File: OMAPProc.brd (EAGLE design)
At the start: 49.8 x 23.2 mm, 11 parts

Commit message: Pre-reinstall commit
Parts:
- removed C30, C31, C32, C33: 0.1uF, SparkFun:0402-CAP
- removed JP11: MPCS6PH, stan:MOLEX-PICO_CLASP_S6P
- removed R18: 4.7k, rcl:R0402
- removed R19, R20: 1.5k, rcl:R0402
- removed SHIFT1: TXS0108E, user:PW_R-PDSO-G20
- added C1, C15, C16, C17, C18, C19, C2, C21, C22, C3, C8: 0.1uF, biomimetic:0402-CAP
- added C10, C11, C12, C13, C14, C4, C5, C6, C9: 1uF, biomimetic:0402-CAP
- added C20: (no value), biomimetic:0603-CAP
- added C7: 22uF, biomimetic:0603-CAP
- added CAM2: ECAM50_5642_MOD, biomimetic:XF2W-2415-1A
- added IC1: MIC5335-SPYMT, biomimetic:MLF-6
- added IC2: MIC5335-MGYMT, biomimetic:MLF-6
- added IC3: TXS0108ERGY, biomimetic:R-PVQFN-N20
- added JP1: Console, biomimetic:MOLEX_503480-0600
- added JP2: ImageProc, biomimetic:MOLEX_503480-0600
- added R1, R2: 1.5k, biomimetic:0402-RES
- added R3, R4, R5, R6, R7: 10k, biomimetic:0402-RES
- added R8: DNP, biomimetic:0402-RES
- added S1: SW_RESET, SparkFun-Electromechanical:TACTILE-SWITCH-1101NE
- added S2: SW_PWRON, SparkFun-Electromechanical:TACTILE-SWITCH-1101NE
- added SDCARD1: MICROSD, biomimetic:AVX_045138008010890+
- CAM1: value AXK7L28227G(LI-VM01CM) -> LI-VM01CM; device user:AXK7L28227G -> biomimetic:AXK7L28227G
- moved SOM1 29.8 mm to (35.8, 11.7), turned to 0 degrees
- moved CAM1 0.89 mm to (9.75, 11.3)
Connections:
- removed net N$18: SHIFT1.20
- removed net N$22: SHIFT1.18
- removed net N$27: SHIFT1.17
- removed net N$30: SHIFT1.16
- removed net N$31: SHIFT1.15
- removed net N$33: SHIFT1.14
- removed net N$34: SHIFT1.13
- removed net N$35: SHIFT1.12
- removed net OMAP_1.8V: C30.1, C32.1, CAM1.10, CAM1.11, R18.2, R19.2, R20.2, SHIFT1.10, SHIFT1.2
- removed net OMAP_3.0V: C31.2, CAM1.13
- removed net OMAP_3.3V: C33.1, SHIFT1.19
- removed net OMAP_GND: C30.2, C31.1, C32.2, C33.2, CAM1.12, CAM1.17, JP11.2, R18.1, SHIFT1.11
- removed net OMAP_SPI2_CLK: SHIFT1.1
- removed net OMAP_SPI2_CS0: SHIFT1.5
- removed net OMAP_SPI2_CS1: SHIFT1.6
- removed net OMAP_SPI2_IRQ: SHIFT1.7
- removed net OMAP_SPI2_SIMO: SHIFT1.3
- removed net OMAP_SPI2_SOMI: SHIFT1.4
- removed net OMAP_SPI4_CLK: SHIFT1.8
- removed net OMAP_SPI4_SIMO: SHIFT1.9
- removed net TERMINAL_CTS: JP11.6
- removed net TERMINAL_RTS: JP11.5
- removed net TERMINAL_RX: JP11.3
- removed net TERMINAL_TX: JP11.4
- removed net V-: SOM1.J1.100, SOM1.J1.12, SOM1.J1.17, SOM1.J1.22, SOM1.J1.27, SOM1.J1.61, SOM1.J1.85, SOM1.J2.1, SOM1.J2.2, SOM1.J2.27, SOM1.J2.30, SOM1.J2.59, SOM1.J2.62, SOM1.J2.90, SOM1.J2.99
- new net !RESET: CAM1.20, CAM2.6, SOM1.J2.6
- new net 1.8V: C1.2, C11.1, C15.1, C19.1, C2.1, C4.1, C5.2, CAM1.10, CAM1.11, CAM2.11, IC2.5, IC3.10, IC3.2, R1.1, R2.1
- new net 2.8V: C10.1, C18.1, C3.1, C6.1, CAM1.13, CAM2.4, IC2.6
- new net 3.0V: C14.1, IC1.5
- new net 3.3V: C13.1, C16.1, C17.1, CAM2.23, IC1.6, IC3.19
- new net GND: C1.1, C10.2, C11.2, C12.1, C13.2, C14.2, C15.2, C16.2, C17.2, C18.2, C19.2, C2.2, C20.2, C21.2, C22.2, C3.2, C4.2, C5.1, C6.2, C7.2, C8.2, C9.1, CAM1.12, CAM1.17, CAM1.21, CAM2.15, CAM2.2, CAM2.24, CAM2.8, IC1.2, IC1.EPAD, IC2.2, IC2.EPAD, IC3.11, IC3.EPAD, JP1.1, JP2.3, JP2.5, SDCARD1.6, SDCARD1.CASE1, SDCARD1.CASE2, SDCARD1.CASE3, SDCARD1.CASE4, SDCARD1.COM, SOM1.J1.100, SOM1.J1.12, SOM1.J1.17, SOM1.J1.22, SOM1.J1.27, SOM1.J1.61, SOM1.J1.85, SOM1.J2.1, SOM1.J2.2, SOM1.J2.27, SOM1.J2.30, SOM1.J2.59, SOM1.J2.62, SOM1.J2.90, SOM1.J2.99
- new net MSTR_NRST: C21.1, S1.P$1, SOM1.J2.92
- new net N$3: S1.P$2, S2.P$2
- new net PWRON: C22.1, S2.P$1, SOM1.J1.5
- new net SD1_CD: R8.1, SDCARD1.CD, SOM1.J2.54
- new net SD1_CLK: SDCARD1.5, SOM1.J2.32
- new net SD1_CMD: R3.1, SDCARD1.3, SOM1.J2.42
- new net SD1_DATA0: R4.1, SDCARD1.7, SOM1.J2.48
- new net SD1_DATA1: R5.1, SDCARD1.8, SOM1.J2.46
- new net SD1_DATA2: R6.1, SDCARD1.1, SOM1.J2.44
- new net SD1_DATA3: R7.1, SDCARD1.2, SOM1.J2.50
- new net UARTA_CTS: JP1.6, SOM1.J1.68
- new net UARTA_RTS: JP1.2, SOM1.J1.74
- new net UARTA_RX: JP1.4, SOM1.J1.70
- new net UARTA_TX: JP1.5, SOM1.J1.72
- new net UARTB_RX: IC3.3, SOM1.J2.41
- new net UARTB_RX_3V3: IC3.18, JP2.4
- new net UARTB_TX: IC3.1, SOM1.J2.43
- new net UARTB_TX_3V3: IC3.20, JP2.6
- new net VMMC1: C7.1, C8.1, R3.2, R4.2, R5.2, R6.2, R7.2, R8.2, SDCARD1.4, SOM1.J1.3
- new net V_BATT: C12.2, C20.1, C9.2, IC1.1, IC1.3, IC1.4, IC2.1, IC2.3, IC2.4, JP2.1, JP2.2, SOM1.J1.14, SOM1.J1.16, SOM1.J1.18, SOM1.J1.20
- net CAM_D0: now also CAM2.19, SOM1.J2.85
- net CAM_D1: now also CAM2.21, SOM1.J2.87
- net CAM_D2: now also CAM2.22, SOM1.J2.31
- net CAM_D3: now also CAM2.20, SOM1.J2.33
- net CAM_D4: now also CAM2.18, SOM1.J2.35
- net CAM_D5: now also CAM2.16, SOM1.J2.29
- net CAM_D6: now also CAM2.14, SOM1.J2.57
- net CAM_D7: now also CAM2.12, SOM1.J2.55
- net CAM_HSYNC: now also CAM2.9, SOM1.J2.63
- net CAM_MCLK: now also CAM2.13, SOM1.J2.71
- net CAM_PCLK: now also CAM2.17, SOM1.J2.67
- net CAM_SCLK: now also CAM2.5, R1.2, SOM1.J2.93; no longer R20.1
- net CAM_SDATA: now also CAM2.3, R2.2, SOM1.J2.91; no longer R19.1
- net CAM_VSYNC: now also CAM2.7, SOM1.J2.65
- net V+: no longer SOM1.J1.14, SOM1.J1.16, SOM1.J1.18, SOM1.J1.20
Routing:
- net OMAP_GND: track 122.0 -> 0.00 mm, vias 14 -> 0
- net OMAP_1.8V: track 82.2 -> 0.00 mm, vias 8 -> 0
- net OMAP_3.0V: track 57.1 -> 0.00 mm, vias 3 -> 0
- net CAM_SDATA: track 43.2 -> 0.00 mm, vias 4 -> 0
- net OMAP_3.3V: track 42.7 -> 0.00 mm, vias 4 -> 0
- net CAM_D7: track 38.4 -> 0.00 mm, vias 4 -> 0
- net CAM_HSYNC: track 38.0 -> 0.00 mm, vias 1 -> 0
- net CAM_MCLK: track 33.7 -> 0.00 mm, vias 1 -> 0
- net CAM_SCLK: track 32.3 -> 0.00 mm, vias 2 -> 0
- net CAM_D5: track 31.8 -> 0.00 mm, vias 3 -> 0
- net CAM_D3: track 30.6 -> 0.00 mm, vias 1 -> 0
- net CAM_D4: track 30.0 -> 0.00 mm, vias 1 -> 0
- net CAM_D2: track 29.7 -> 0.00 mm, vias 1 -> 0
- net CAM_D6: track 25.6 -> 0.00 mm, vias 2 -> 0
- net CAM_VSYNC: track 25.6 -> 0.00 mm, vias 3 -> 0
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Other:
- board text removed: "Berkeley EECS"
- board text removed: "CVProc 0.1"
- board text removed: "Ryan Julian"

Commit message: Near-final placement, partial route
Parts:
- removed C18, C19, C2: 0.1uF, biomimetic:0402-CAP
- removed C4: 1uF, biomimetic:0402-CAP
- moved C6 46.3 mm to (36.5, 18.0), flipped to the bottom, turned to 90 degrees
- moved R8 44.6 mm to (5.94, 5.79), flipped to the bottom, turned to 270 degrees
- moved C17 42.6 mm to (38.2, 5.71), flipped to the bottom, turned to 270 degrees
- moved C5 39.3 mm to (36.5, 12.2), flipped to the bottom, turned to 90 degrees
- moved CAM2 39.2 mm to (41.3, 11.6), turned to 270 degrees
- moved C7 37.9 mm to (23.2, 20.9), flipped to the bottom, turned to 90 degrees
- moved C3 37.8 mm to (35.1, 18.0), flipped to the bottom, turned to 90 degrees
- moved R1 37.1 mm to (30.1, 17.4), flipped to the bottom, turned to 270 degrees
- moved R6 35.7 mm to (22.2, 15.5), flipped to the bottom, turned to 270 degrees
- moved C8 34.7 mm to (24.8, 15.1), flipped to the bottom, turned to 270 degrees
- moved C22 33.6 mm to (9.09, 26.2), flipped to the bottom
- moved SDCARD1 33.2 mm to (8.23, 14.3), turned to 270 degrees
- moved S1 33.1 mm to (1.60, -2.97), turned to 180 degrees
- moved R7 32.5 mm to (22.2, 8.99), flipped to the bottom, turned to 90 degrees
- moved R3 32.0 mm to (21.3, 18.9), flipped to the bottom, turned to 90 degrees
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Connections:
- net 1.8V: no longer C19.1, C2.1, C4.1
- net 2.8V: no longer C18.1
- net GND: no longer C18.2, C19.2, C2.2, C4.2
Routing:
- net CAM_SDATA: track 0.00 -> 51.6 mm, vias 0 -> 3
- net CAM_SCLK: track 0.00 -> 46.3 mm, vias 0 -> 3
- net CAM_D0: track 0.00 -> 45.9 mm, vias 0 -> 3
- net CAM_D1: track 0.00 -> 44.3 mm, vias 0 -> 3
- net CAM_MCLK: track 0.00 -> 41.7 mm, vias 0 -> 3
- net CAM_HSYNC: track 0.00 -> 38.1 mm, vias 0 -> 3
- net CAM_PCLK: track 0.00 -> 37.2 mm, vias 0 -> 3
- net CAM_D7: track 0.00 -> 36.7 mm, vias 0 -> 3
- net CAM_D6: track 0.00 -> 33.4 mm, vias 0 -> 3
- net CAM_D4: track 0.00 -> 32.9 mm, vias 0 -> 3
- net CAM_D2: track 0.00 -> 31.8 mm, vias 0 -> 3
- net CAM_D5: track 0.00 -> 31.1 mm, vias 0 -> 3
- net CAM_D3: track 0.00 -> 29.6 mm, vias 0 -> 3
- net SD1_DATA2: track 0.00 -> 24.4 mm, vias 0 -> 1
- net SD1_CMD: track 0.00 -> 20.9 mm, vias 0 -> 1
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- added copper zone on layer 1, net GND
- added copper zone on layer 16, net GND
- added copper zone on layer 2, net GND
- added copper zone on layer 3, net V_BATT
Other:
- board size 49.8 x 23.2 mm -> 44.5 x 23.2 mm

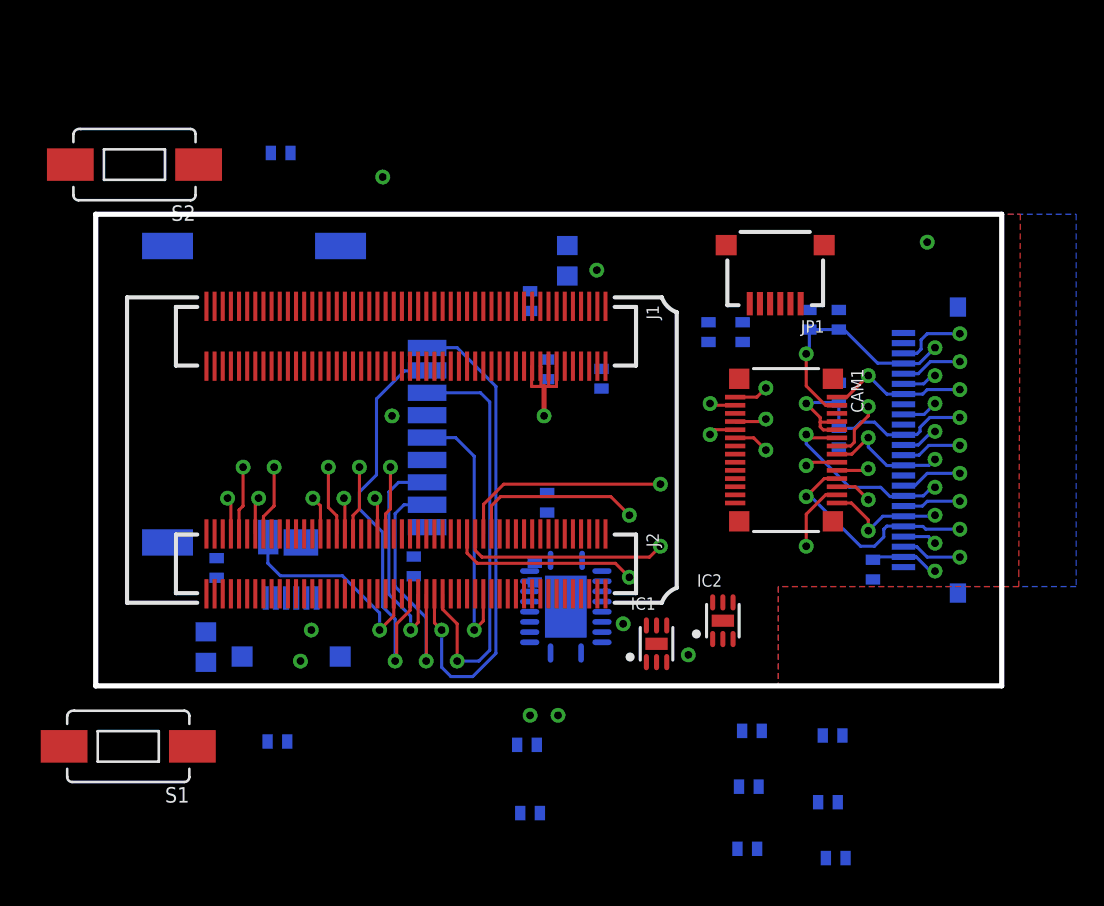
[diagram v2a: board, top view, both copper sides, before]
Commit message: SD card routing complete
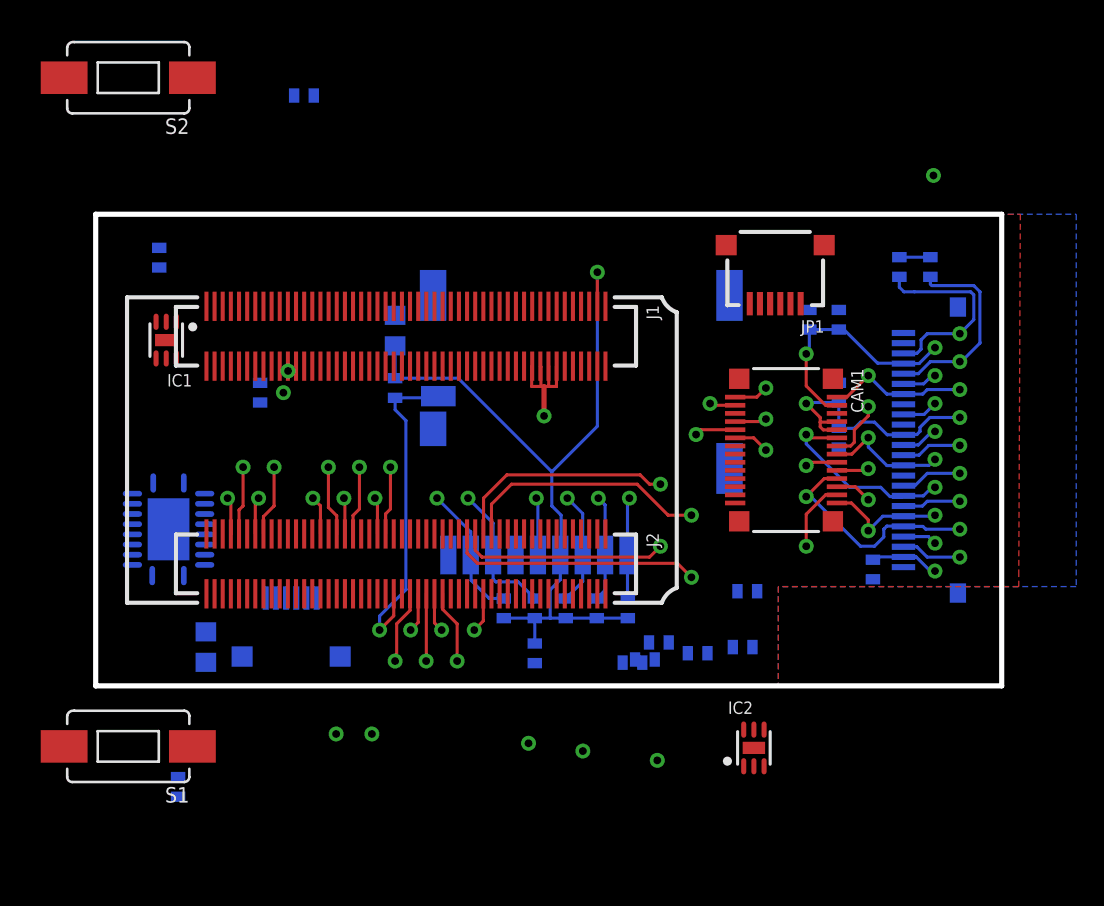
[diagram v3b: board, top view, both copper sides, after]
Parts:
- moved C15 30.0 mm to (3.12, 21.0), turned to 90 degrees
- moved IC1 28.3 mm to (3.47, 17.0), turned to 180 degrees
- moved C16 24.5 mm to (8.08, 14.4), turned to 90 degrees
- moved IC3 19.9 mm to (3.58, 7.69), turned to 90 degrees
- moved SDCARD1 15.6 mm to (23.9, 14.5), turned to 0 degrees
- moved R3 15.2 mm to (23.1, 3.81), turned to 270 degrees
- moved C8 13.9 mm to (21.6, 1.60)
- moved R8 12.4 mm to (14.7, 14.6), turned to 90 degrees
- moved R6 12.4 mm to (26.1, 3.81)
- moved R1 11.4 mm to (41.0, 20.6)
- moved C9 11.3 mm to (31.8, 1.91)
- moved C13 11.0 mm to (27.7, 2.13)
- moved C11 10.5 mm to (26.4, 1.14)
- moved C10 9.72 mm to (29.6, 1.60)
- moved C12 9.60 mm to (32.0, 4.65)
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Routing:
- net VMMC1: track 0.00 -> 38.5 mm
- net CAM_SCLK: track 46.3 -> 53.8 mm
- net SD1_DATA1: track 12.9 -> 19.6 mm, vias 1 -> 2
- net CAM_SDATA: track 51.6 -> 58.2 mm
- net SD1_CD: track 10.7 -> 16.4 mm
- net SD1_DATA2: track 24.4 -> 18.8 mm, vias 1 -> 2
- net SD1_DATA0: track 11.2 -> 16.5 mm, vias 1 -> 2
- net CAM_D1: track 44.3 -> 48.4 mm
- net CAM_D0: track 45.9 -> 49.9 mm
- net SD1_DATA3: track 20.6 -> 22.4 mm, vias 1 -> 2
- net 1.8V: track 13.2 -> 14.7 mm
- net SD1_CMD: track 20.9 -> 19.6 mm, vias 1 -> 2
- net SD1_CLK: track 13.2 -> 12.5 mm, vias 1 -> 2
- net CAM_D2: track 31.8 -> 32.4 mm
- net CAM_D5: track 31.1 -> 31.6 mm

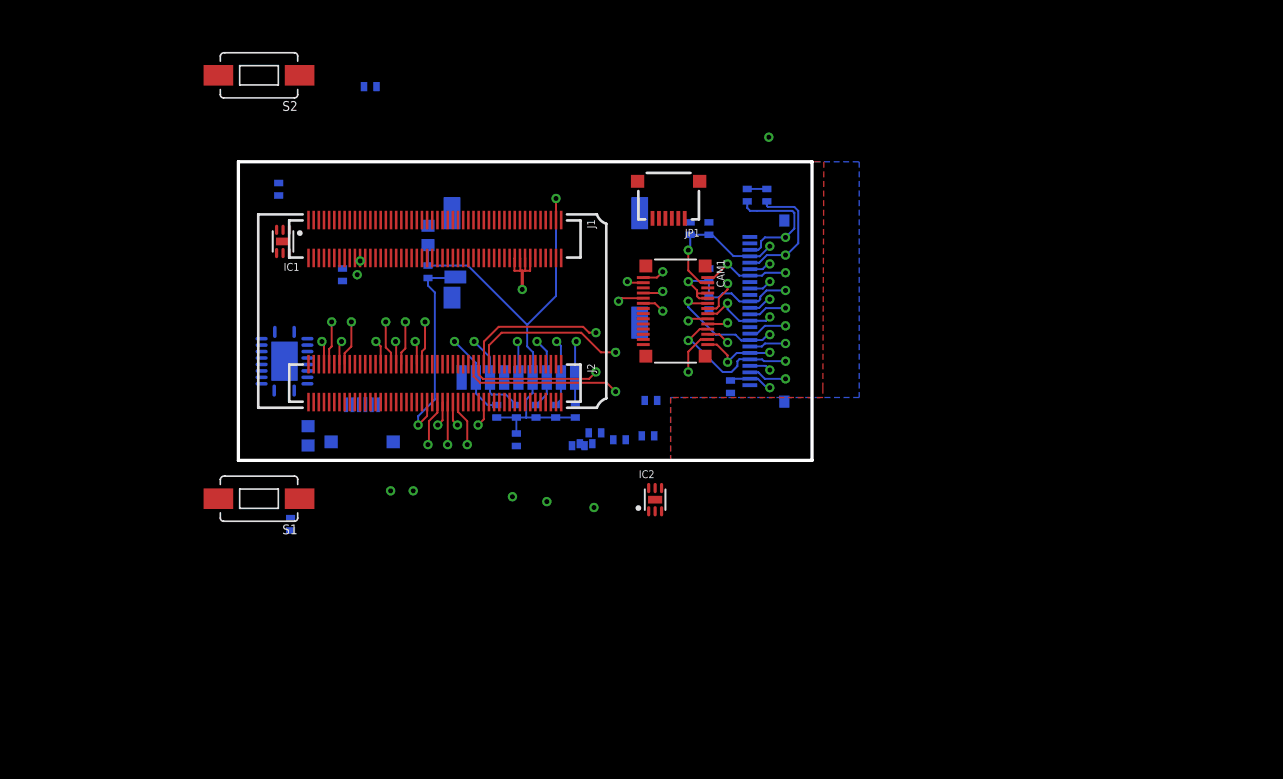
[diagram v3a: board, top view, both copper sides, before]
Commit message: Routing almost complete
Missing switches
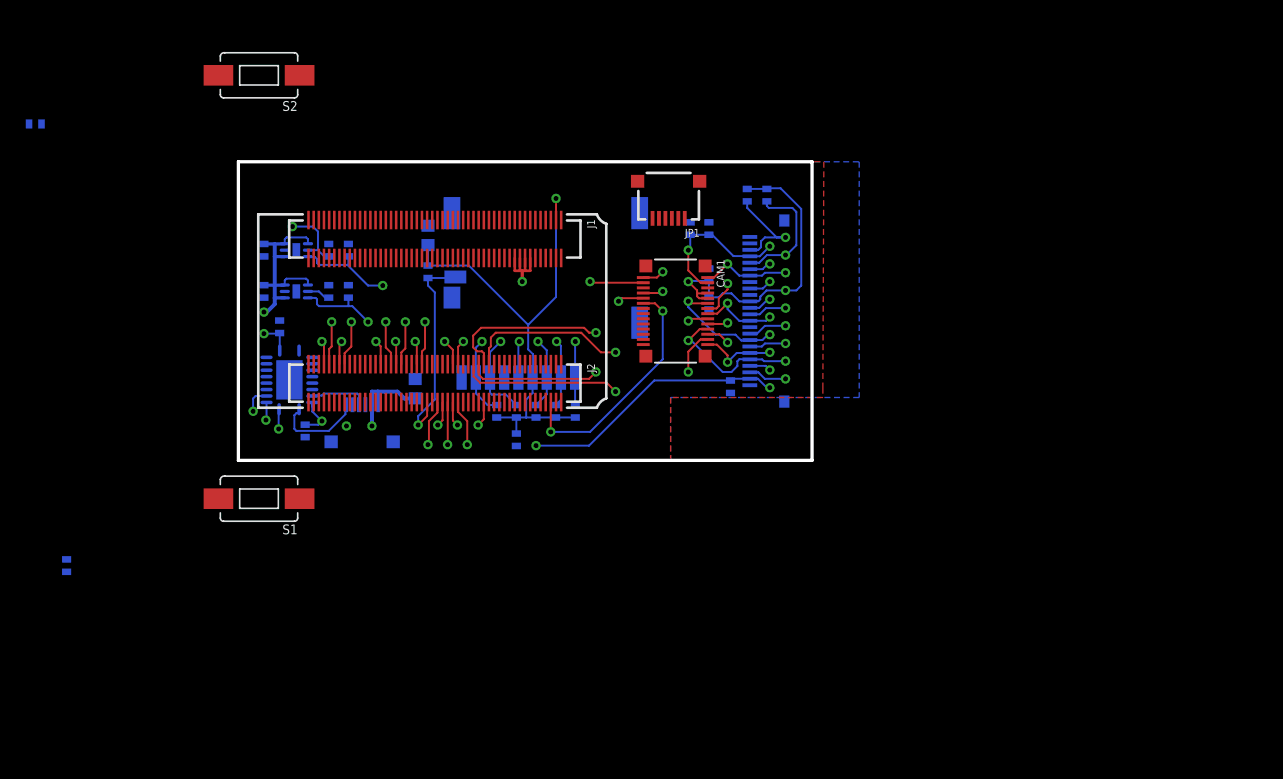
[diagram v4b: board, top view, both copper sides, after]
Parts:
- moved IC2 33.9 mm to (4.50, 16.3), flipped to the bottom, turned to 90 degrees
- moved C9 33.1 mm to (1.98, 16.3), turned to 90 degrees
- moved C12 31.2 mm to (1.98, 13.1), turned to 90 degrees
- moved C22 26.1 mm to (-15.8, 26.1)
- moved C10 25.7 mm to (8.53, 16.3), turned to 90 degrees
- moved C11 24.6 mm to (7.01, 16.3), turned to 90 degrees
- moved C14 23.2 mm to (7.01, 13.1), turned to 90 degrees
- moved C13 22.1 mm to (8.53, 13.1), turned to 90 degrees
- moved C21 17.7 mm to (-13.3, -8.16)
- moved C16 12.5 mm to (5.18, 2.29), turned to 270 degrees
- moved C15 10.7 mm to (3.20, 10.4)
- moved C20 9.08 mm to (13.7, 5.56), turned to 90 degrees
- moved IC1 4.01 mm to (4.50, 13.1), flipped to the bottom, turned to 90 degrees
- moved IC3 1.50 mm to (3.96, 6.24)
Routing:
- net 3.3V: track 3.39 -> 57.5 mm, vias 1 -> 4
- net 1.8V: track 14.7 -> 50.8 mm, vias 2 -> 5
- net CAM_VSYNC: track 8.72 -> 44.3 mm
- net 2.8V: track 11.9 -> 44.4 mm, vias 2 -> 3
- net UARTB_RX: track 0.00 -> 25.8 mm, vias 1 -> 2
- net V_BATT: track 6.68 -> 29.2 mm
- net UARTB_TX: track 0.00 -> 19.3 mm, vias 1 -> 2
- net !RESET: track 13.3 -> 30.4 mm
- net UARTB_TX_3V3: track 0.00 -> 7.17 mm
- net UARTB_RX_3V3: track 0.00 -> 4.51 mm
- net CAM_MCLK: track 41.7 -> 45.3 mm
- net CAM_SDATA: track 58.2 -> 56.1 mm
- net 3.0V: track 0.00 -> 1.81 mm
- net CAM_D2: track 32.4 -> 34.0 mm
- net SD1_DATA0: track 16.5 -> 17.2 mm

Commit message: Routing and silkscreen complete.
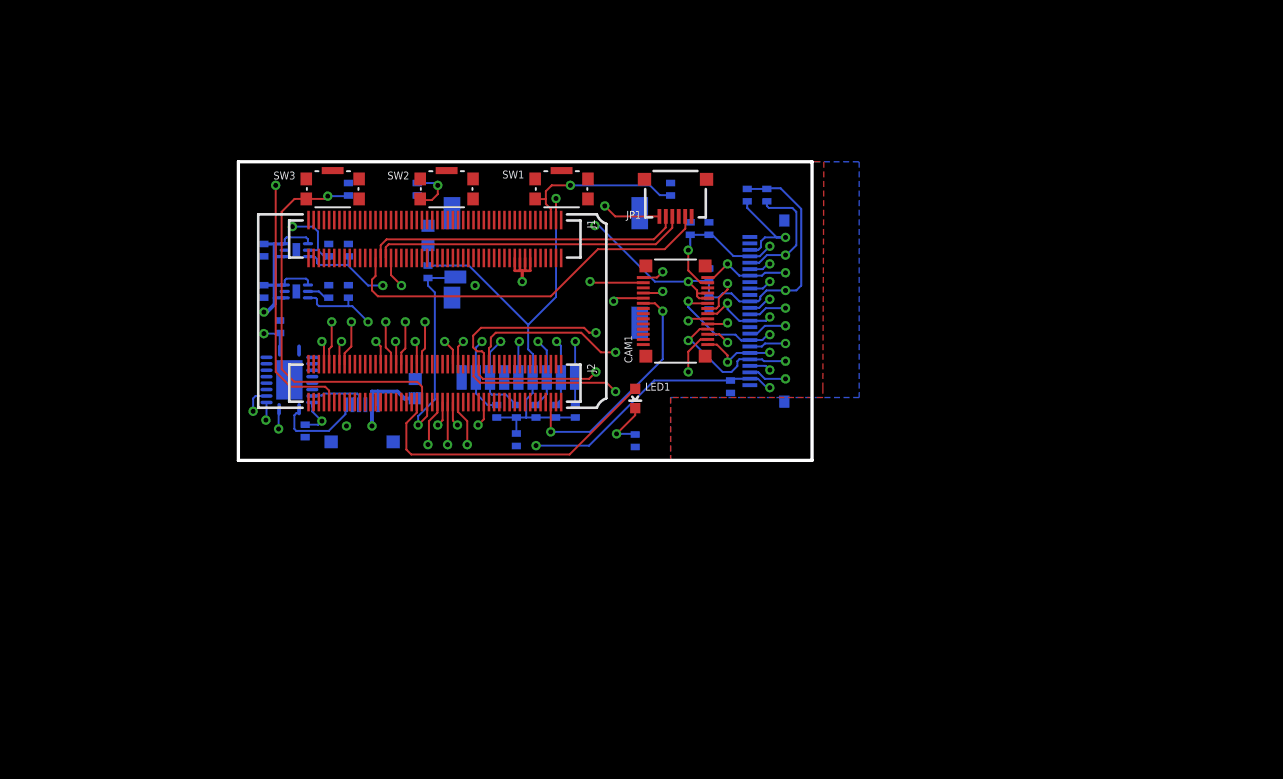
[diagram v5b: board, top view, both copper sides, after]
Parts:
- removed S1: SW_RESET, SparkFun-Electromechanical:TACTILE-SWITCH-1101NE
- removed S2: SW_PWRON, SparkFun-Electromechanical:TACTILE-SWITCH-1101NE
- added C2: 0.1uF, biomimetic:0402-CAP
- added LED1: USER, biomimetic:LED-0603
- added R9: 330, biomimetic:0402-RES
- added SW1: PWRON, biomimetic:KMR421G
- added SW2: RESET, biomimetic:KMR421G
- added SW3: USER, biomimetic:KMR421G
- C20: value (none) -> 22uF
- JP1: value Console -> CONSOLE
- JP2: value ImageProc -> IMAGEPROC
- moved C22 49.5 mm to (33.5, 21.0), turned to 90 degrees
- moved C21 39.9 mm to (13.9, 21.0), turned to 270 degrees
- moved JP1 0.55 mm to (33.9, 20.7)
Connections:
- removed net V+: SOM1.J1.24, SOM1.J2.4, SOM1.J2.7
- new net N$1: SOM1.J1.24
- new net N$2: SOM1.J2.4, SOM1.J2.7
- new net USER_LED: LED1.A, SOM1.J2.58
- new net USER_SW: C2.1, SOM1.J2.56, SW3.1, SW3.2
- net GND: now also C2.2, R9.2, SW1.3, SW1.4, SW1.CASE, SW2.3, SW2.4, SW2.CASE, SW3.3, SW3.4, SW3.CASE
- net MSTR_NRST: now also SW2.1, SW2.2; no longer S1.P$1
- net N$3: now also LED1.C, R9.1; no longer S1.P$2, S2.P$2
- net PWRON: now also SW1.1, SW1.2; no longer S2.P$1
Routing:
- net MSTR_NRST: track 0.00 -> 37.1 mm, vias 0 -> 2
- net 1.8V: track 50.8 -> 83.4 mm, vias 5 -> 6
- net USER_SW: track 0.00 -> 30.6 mm, vias 0 -> 1
- net UARTA_RTS: track 0.00 -> 30.3 mm
- net UARTA_CTS: track 0.00 -> 25.4 mm, vias 0 -> 2
- net UARTA_RX: track 0.00 -> 24.6 mm
- net UARTA_TX: track 0.00 -> 24.5 mm
- net USER_LED: track 0.00 -> 24.0 mm
- net PWRON: track 0.00 -> 13.4 mm, vias 0 -> 1
- net N$3: track 0.00 -> 4.09 mm, vias 0 -> 1
- net CAM_SDATA: track 56.1 -> 53.6 mm
